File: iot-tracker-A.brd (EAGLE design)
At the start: 21.6 x 19.6 mm, 27 parts, among them Q1 MMBT3906, U1 ESP-WROOM-02, U2 PCF85263ATL_AX, U3 TPS61021ADSGR, Y1 32.768kHz

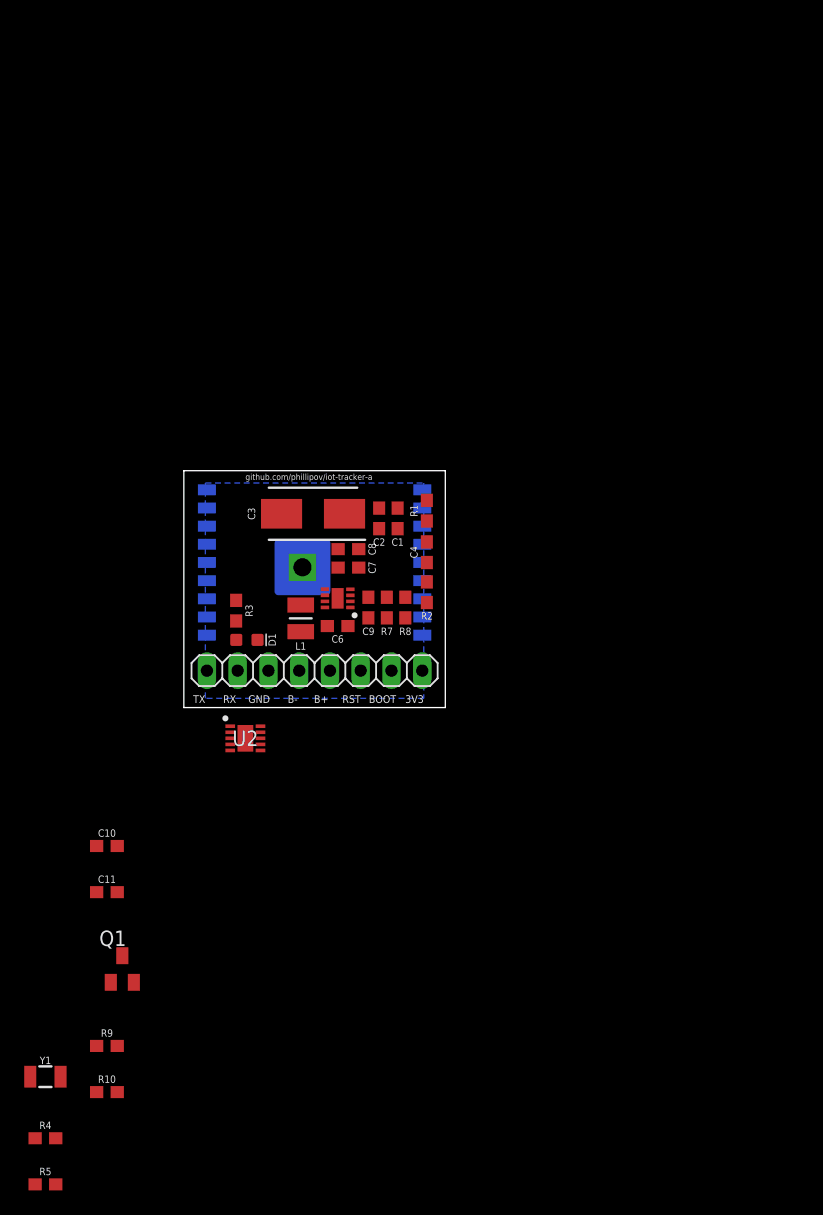
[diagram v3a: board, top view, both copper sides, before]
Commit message: Reordered names and grouped components on the board
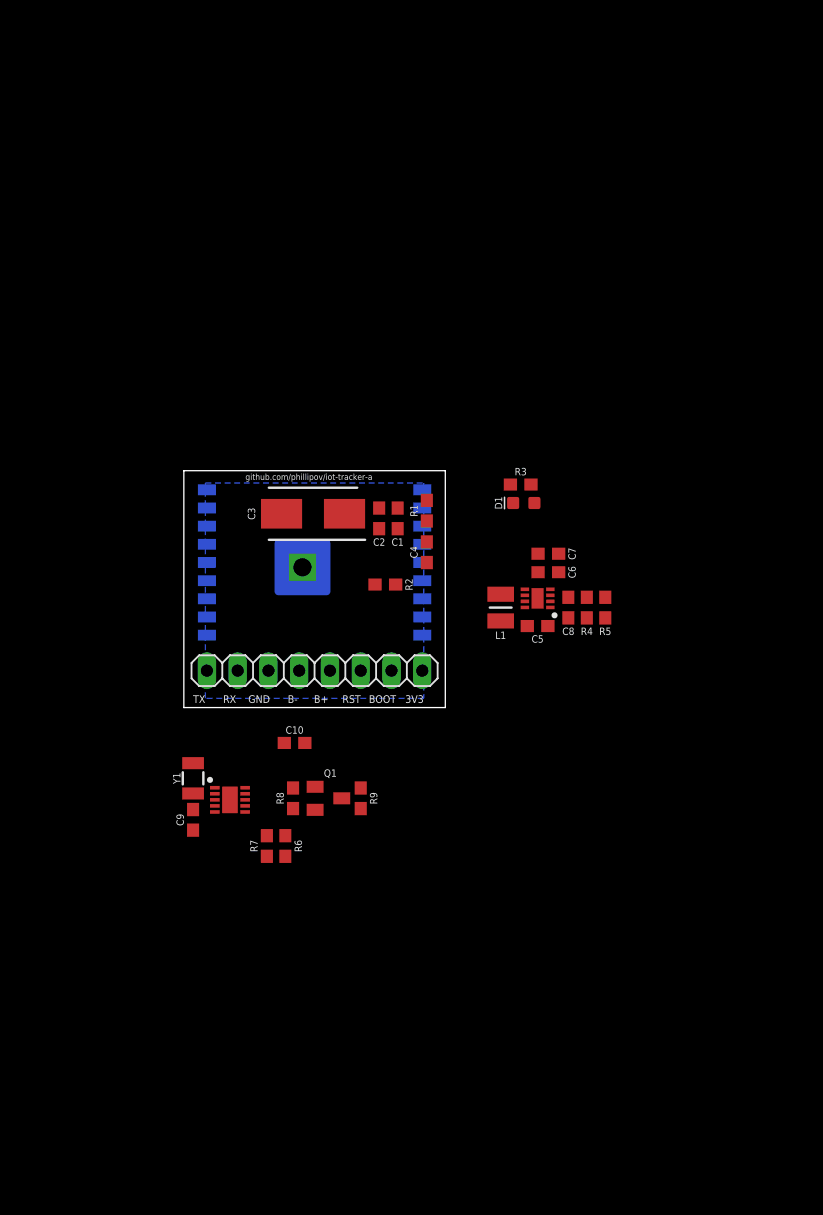
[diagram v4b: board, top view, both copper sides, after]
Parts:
- removed C11: 0.1uF, SparkFun-Capacitors:0603
- removed R10: 100k, SparkFun-Resistors:0603
- added C5: 10uF, SparkFun-Capacitors:0603
- added R6: 4.7k, SparkFun-Resistors:0603
- C8: value 10uF -> 10pF
- C9: value 10pF -> 0.1uF
- R4: value 4.7k -> 316k
- R5: value 4.7k -> 100k
- R7: value 316k -> 4.7k
- U2: value PCF85263ATL_AX -> TPS61021ADSGR; device IOT-Tracker-A:SON50P260X260X50-11N -> IOT-Tracker-A:SON50P200X200X80-9N
- U3: value TPS61021ADSGR -> PCF85263ATL_AX; device IOT-Tracker-A:SON50P200X200X80-9N -> IOT-Tracker-A:SON50P260X260X50-11N
- moved R5 66.4 mm to (34.8, 8.26), turned to 90 degrees
- moved R4 62.6 mm to (33.3, 8.26), turned to 270 degrees
- moved R9 29.3 mm to (14.6, -7.49), turned to 90 degrees
- moved Y1 27.5 mm to (0.76, -5.84), turned to 90 degrees
- moved U2 26.8 mm to (29.2, 9.02), turned to 180 degrees
- moved R3 25.7 mm to (27.8, 18.4), turned to 0 degrees
- moved D1 25.5 mm to (28.1, 16.9), turned to 180 degrees
- moved C9 22.7 mm to (0.76, -9.27)
- moved Q1 22.1 mm to (11.9, -7.49), turned to 270 degrees
- moved R7 22.0 mm to (6.86, -11.4)
- moved U3 18.9 mm to (3.81, -7.62), turned to 0 degrees
- moved C8 18.8 mm to (31.8, 8.26), turned to 90 degrees
- moved R8 18.3 mm to (9.02, -7.49)
- moved C6 18.0 mm to (30.1, 11.2), turned to 180 degrees
- moved C10 17.7 mm to (9.14, -2.92), turned to 180 degrees
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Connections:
- net 3.3V: now also C10.2, C6.1, C8.2, R4.1, R6.2, R7.2, U2.3, U2.4, U3.10; no longer C11.2, C8.1, C9.2, R4.2, R5.2, R7.1, U2.10, U3.3, U3.4
- net DRVN: now also R9.2, U2.5; no longer R10.2, U3.5
- net FB: now also C8.1, R4.2, R5.1, U2.2; no longer C9.1, R7.2, R8.1, U3.2
- net GND: now also C5.2, C9.1, R5.2, R9.1, U2.1, U2.9, U3.5; no longer C11.1, C8.2, R10.1, R8.2, U2.5, U3.1, U3.9
- net INTA: now also R8.1, U3.9; no longer R9.1, U2.9
- net INTA_PNP_B: now also R8.2; no longer R9.2
- net OSCI: now also U3.1; no longer U2.1
- net OSCO: now also U3.2; no longer U2.2
- net SCL: now also R6.1, U3.7; no longer R4.1, U2.7
- net SDA: now also R7.1, U3.6; no longer R5.1, U2.6
- net SW: now also U2.6, U2.7; no longer U3.6, U3.7
- net V_BATT: now also C5.1, C9.2, U2.8, U3.3; no longer C10.2, C6.1, U2.3, U3.8

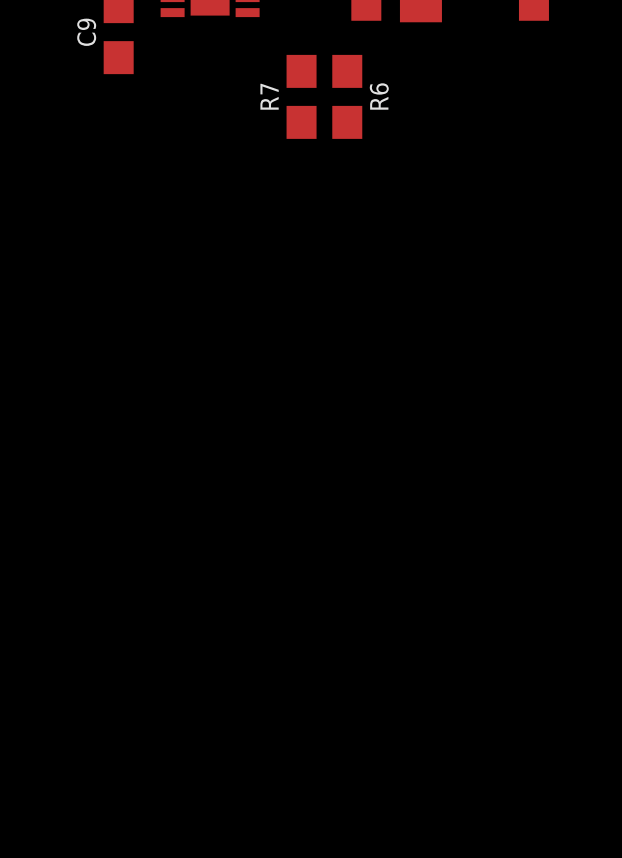
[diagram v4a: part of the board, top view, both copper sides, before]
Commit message: Added buttons for reset and boot options
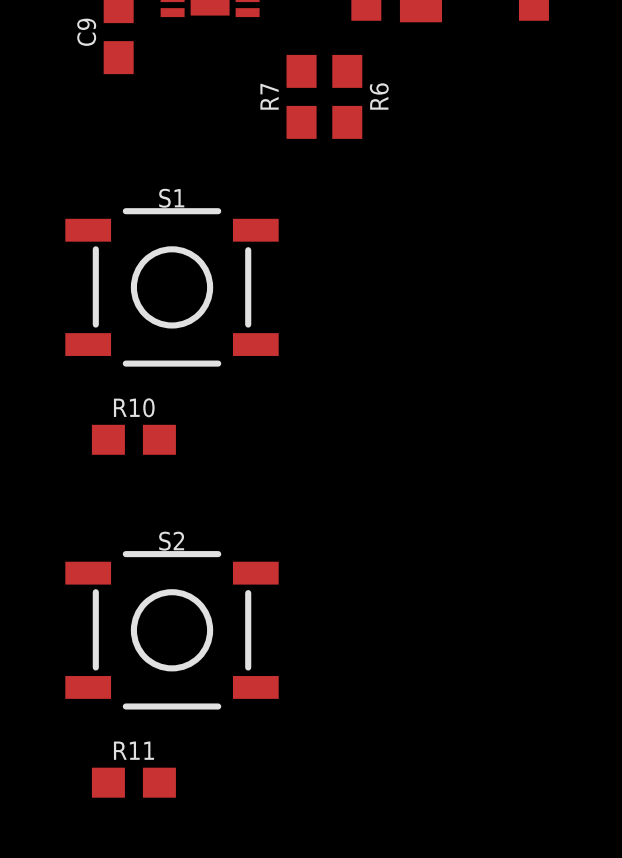
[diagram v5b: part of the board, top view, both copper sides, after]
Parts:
- added R10, R11: 10k, SparkFun-Resistors:0603
- added S1, S2: (no value), SparkFun-Switches:TACTILE_SWITCH_SMD_5.2MM
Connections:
- net 3.3V: now also R10.2, R11.2
- net BOOT: now also R11.1, S2.1
- net GND: now also S1.3, S2.3
- net RST: now also R10.1, S1.1

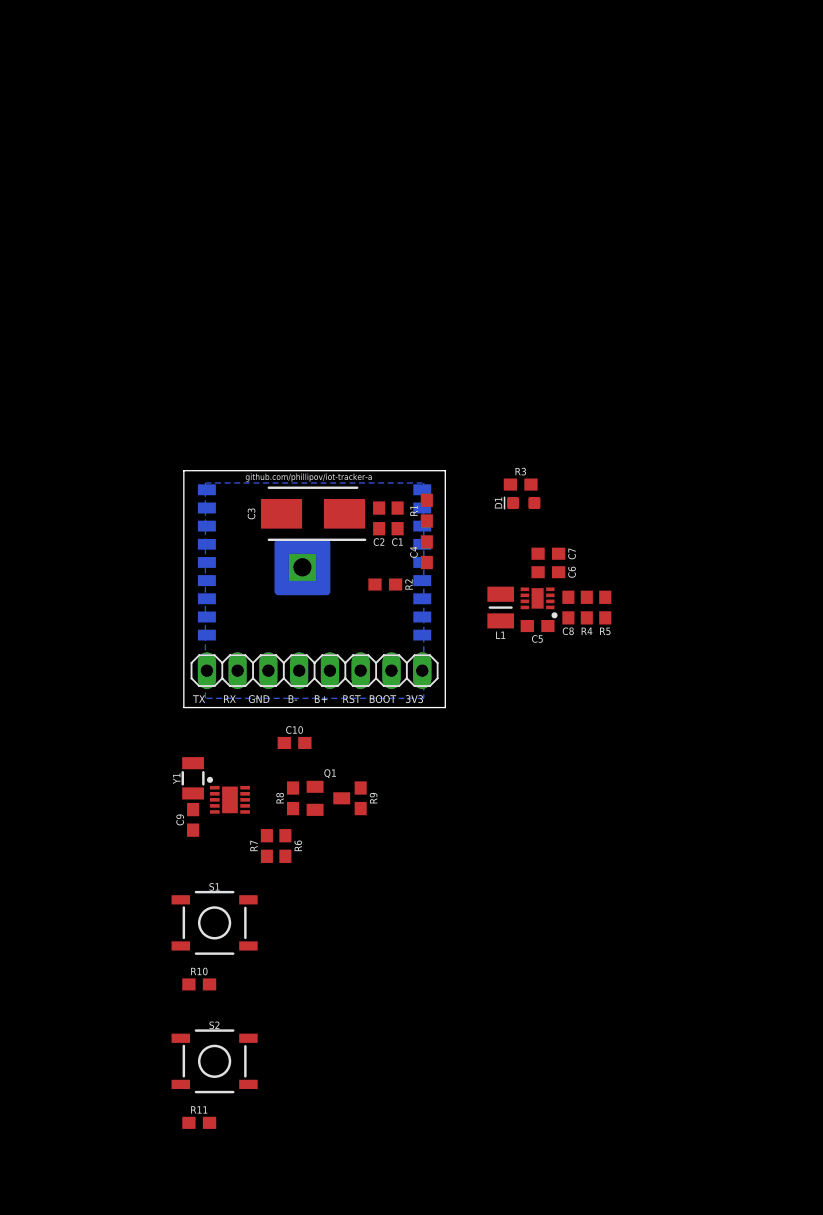
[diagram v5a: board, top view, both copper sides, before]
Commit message: Replaced 1x8 header with buttons, screw terminals, and a 1x4 header
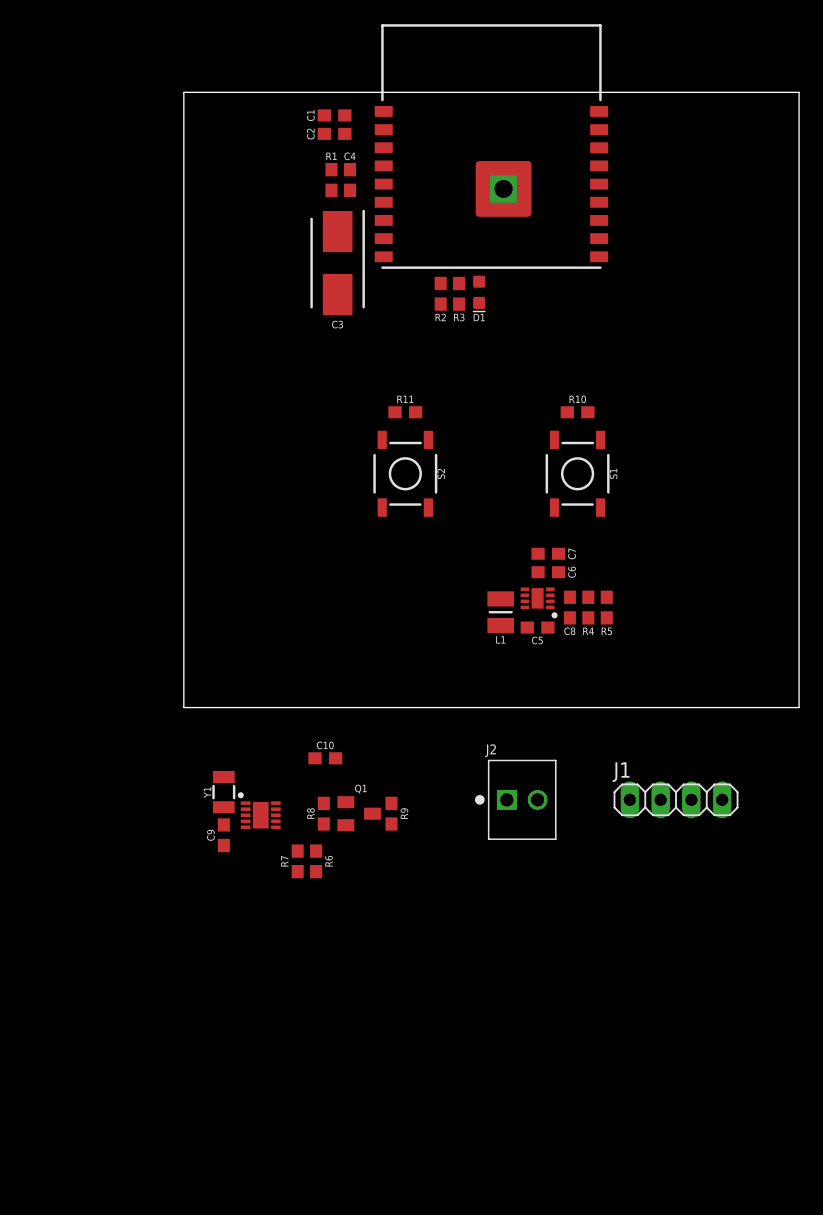
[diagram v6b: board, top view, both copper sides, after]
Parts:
- removed JP1: (no value), pinhead:1X08
- added J1: (no value), pinhead:1X04
- added J2: 282834-2, IOT-Tracker-A:CONN_282834-2
- moved R11 61.1 mm to (18.3, 24.4), turned to 180 degrees
- moved R10 56.6 mm to (32.5, 24.4), turned to 180 degrees
- moved S2 51.0 mm to (18.3, 19.3), turned to 270 degrees
- moved S1 47.7 mm to (32.5, 19.3), turned to 270 degrees
- moved U1 34.5 mm to (25.4, 44.3), flipped to the top
- moved C1 33.7 mm to (12.4, 48.9), turned to 0 degrees
- moved C2 32.0 mm to (12.4, 47.4), turned to 0 degrees
- moved C4 31.4 mm to (13.7, 43.6)
- moved R1 28.4 mm to (12.2, 43.6), turned to 90 degrees
- moved R2 24.4 mm to (21.2, 34.2), turned to 270 degrees
- moved C3 20.8 mm to (12.7, 36.7), turned to 270 degrees
- moved D1 17.8 mm to (24.4, 34.3), turned to 270 degrees
- moved R3 16.5 mm to (22.7, 34.2), turned to 270 degrees
- moved R6 2.84 mm to (10.9, -12.7)
- moved R8 2.84 mm to (11.6, -8.76)
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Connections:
- net 3.3V: now also J1.1, J2.1; no longer JP1.1
- net BOOT: no longer JP1.2
- net GND: now also J1.2, J2.2; no longer JP1.5, JP1.6
- net RST: no longer JP1.3
- net RX: now also J1.4; no longer JP1.8
- net TX: now also J1.3; no longer JP1.7
- net V_BATT: no longer JP1.4
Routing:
- removed copper zone on layer 16, net GND
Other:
- board size 21.6 x 19.6 mm -> 50.8 x 50.8 mm
- board text removed: "3V3"
- board text removed: "B+"
- board text removed: "B-"
- board text removed: "BOOT"
- board text removed: "GND"
- board text removed: "RST"
- board text removed: "RX"
- board text removed: "TX"
- board text removed: "github.com/phillipov/iot-tracker-a"

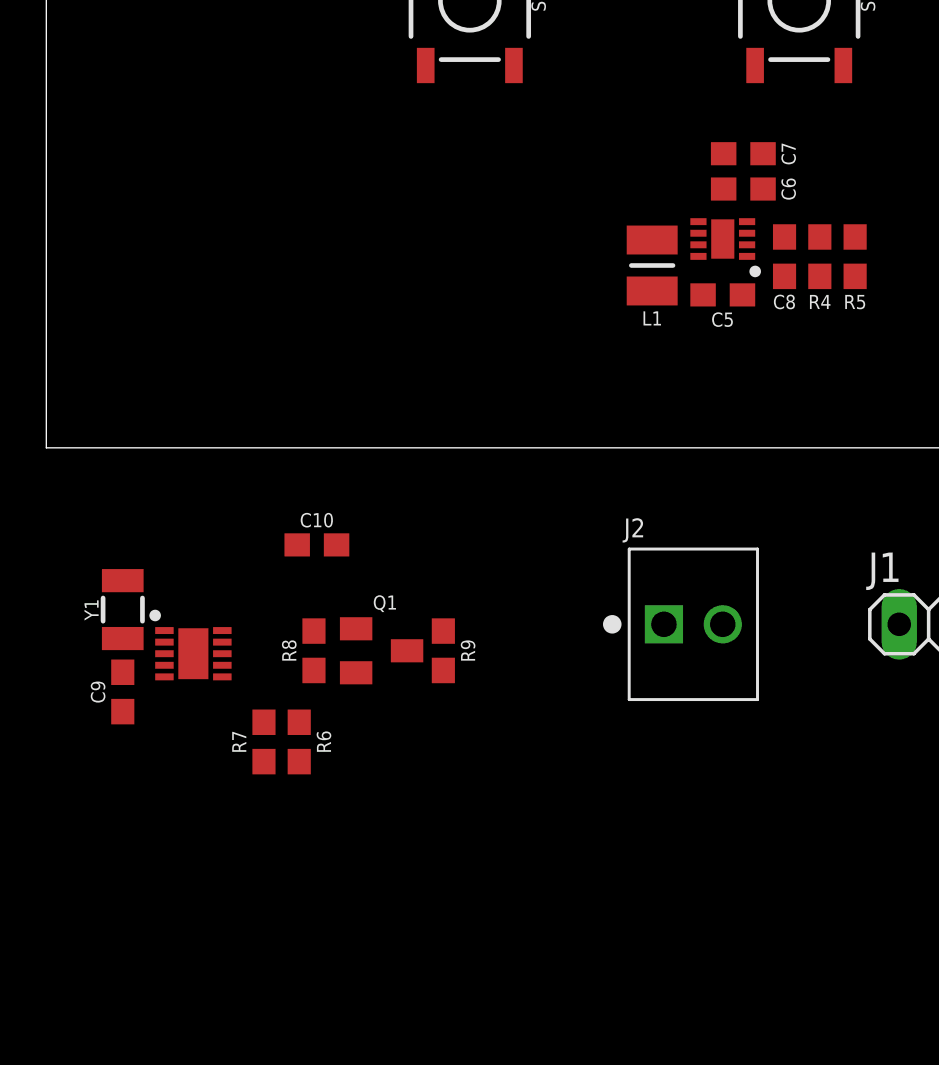
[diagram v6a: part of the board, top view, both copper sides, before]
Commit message: Connected a MOSFET switch and voltage divider to the ADC; connected a capacitor to boost enable pin
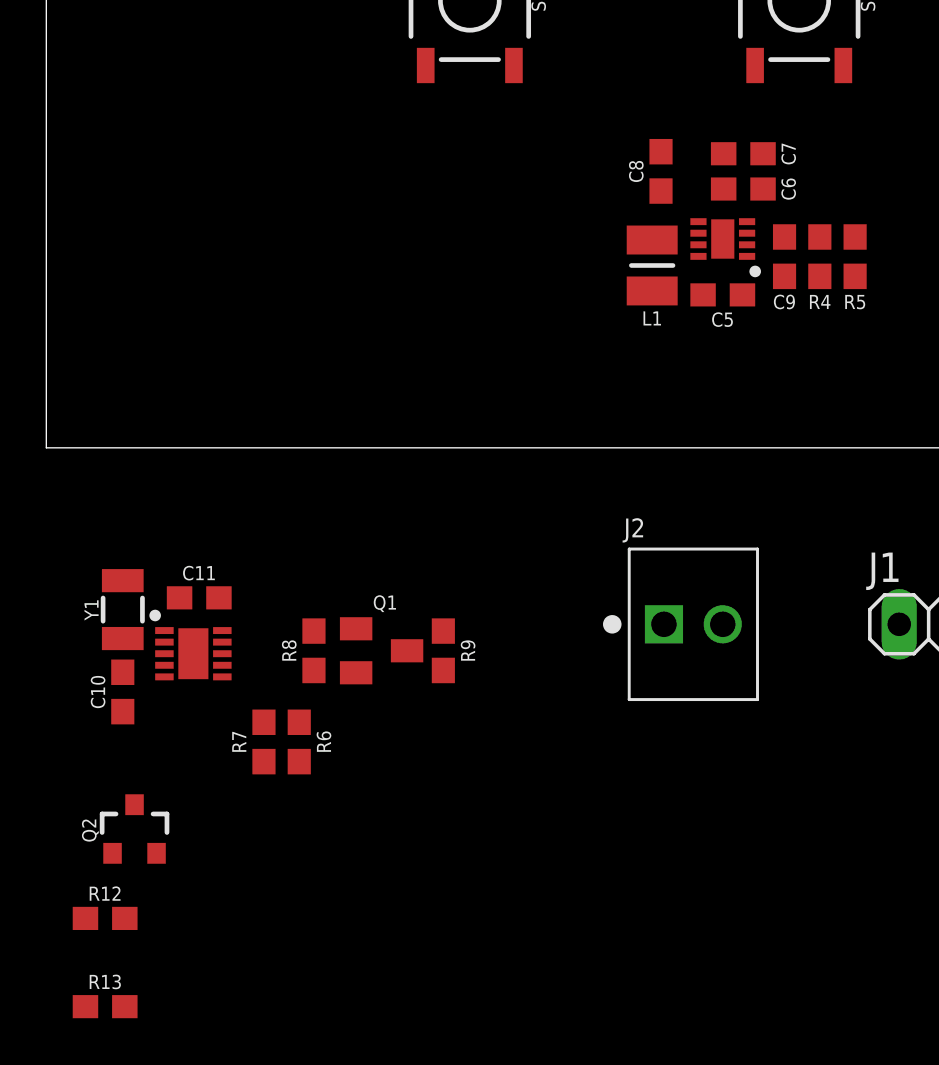
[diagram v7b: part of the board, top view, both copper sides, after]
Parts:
- added C11: 0.1uF, SparkFun-Capacitors:0603
- added Q2: BSS138, SparkFun-DiscreteSemi:SOT23-3
- added R12, R13: 100k, SparkFun-Resistors:0603
- C8: value 10pF -> 0.1uF
- C9: value 0.1uF -> 10pF
- moved C9 34.2 mm to (31.9, 8.26)
- moved C10 10.5 mm to (3.30, -10.5), turned to 90 degrees
- moved C8 6.48 mm to (26.5, 11.9)
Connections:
- net EN renamed ESP_EN
- removed net DRVN: Q1.C, R9.2, U2.5
- new net ADC: R12.1, R13.2, U1.16
- new net BOOST_EN: C8.1, Q1.C, R9.2, U2.5
- new net N$1: Q2.2, R12.2
- net 3.3V: now also C11.2, C9.2, Q2.1; no longer C10.2, C8.2
- net FB: now also C9.1; no longer C8.1
- net GND: now also C10.2, C11.1, C8.2, R13.1; no longer C10.1, C9.1
- net V_BATT: now also C10.1, Q2.3; no longer C9.2
